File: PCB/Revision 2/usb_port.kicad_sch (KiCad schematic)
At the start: 1 part, among them J2 USB_A

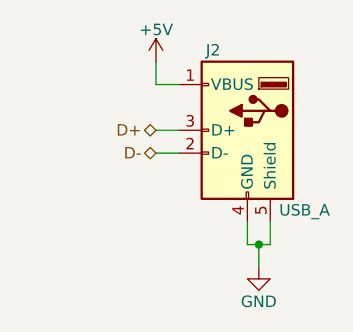
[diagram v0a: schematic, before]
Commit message: ESD protection diodes go BRRRRRRR
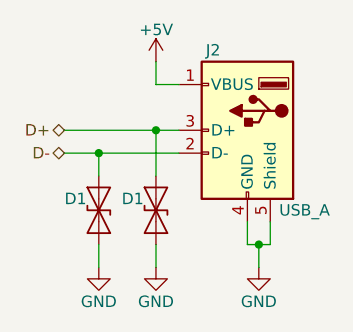
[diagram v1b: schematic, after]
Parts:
- added D1 (x2): ESD9B3.3ST5G, Diode_SMD:D_SOD-923, symbol Diode:ESD9B3.3ST5G
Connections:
- net D+: now also D1.1 (A1)
- net D-: now also D1.1 (A1)
- net GND: now also D1.2 (A2), D1.2 (A2)
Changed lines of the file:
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@@
 (kicad_sch (version 20230121) (generator eeschema)
   (paper "USLetter")
+  (junction (at 128.27 85.09) (diameter 0) (color 0 0 0 0)
+  )
+  (junction (at 121.92 87.63) (diameter 0) (color 0 0 0 0)
+  )
   (junction (at 139.7 97.79) (diameter 0) (color 0 0 0 0)
   )
@@
     (stroke (width 0) (type default))
   )
+  (wire (pts (xy 118.11 85.09) (xy 128.27 85.09))
+    (stroke (width 0) (type default))
+  )
+  (wire (pts (xy 128.27 85.09) (xy 128.27 90.17))
+    (stroke (width 0) (type default))
+  )
+  (wire (pts (xy 121.92 87.63) (xy 121.92 90.17))
+    (stroke (width 0) (type default))
+  )
+  (wire (pts (xy 121.92 97.79) (xy 121.92 100.33))
+    (stroke (width 0) (type default))
+  )
+  (wire (pts (xy 138.43 95.25) (xy 138.43 97.79))
+    (stroke (width 0) (type default))
+  )
+  (wire (pts (xy 118.11 87.63) (xy 121.92 87.63))
+    (stroke (width 0) (type default))
+  )
+  (wire (pts (xy 128.27 97.79) (xy 128.27 100.33))
+    (stroke (width 0) (type default))
+  )
   (wire (pts (xy 128.27 85.09) (xy 130.81 85.09))
     (stroke (width 0) (type default))
   )
-  (wire (pts (xy 138.43 95.25) (xy 138.43 97.79))
-    (stroke (width 0) (type default))
-  )
   (wire (pts (xy 138.43 97.79) (xy 139.7 97.79))
     (stroke (width 0) (type default))
   )
+  (wire (pts (xy 121.92 87.63) (xy 130.81 87.63))
+    (stroke (width 0) (type default))
+  )
   (wire (pts (xy 140.97 95.25) (xy 140.97 97.79))
     (stroke (width 0) (type default))
@@
     (stroke (width 0) (type default))
   )
-  (wire (pts (xy 128.27 87.63) (xy 130.81 87.63))
-    (stroke (width 0) (type default))
-  )
   (wire (pts (xy 128.27 80.01) (xy 130.81 80.01))
     (stroke (width 0) (type default))
@@
     (stroke (width 0) (type default))
   )
-  (hierarchical_label "D-" (shape bidirectional) (at 128.27 87.63 180) (fields_autoplaced)
+  (hierarchical_label "D-" (shape bidirectional) (at 118.11 87.63 180) (fields_autoplaced)
     (effects (font (size 1.27 1.27)) (justify right))
   )
-  (hierarchical_label "D+" (shape bidirectional) (at 128.27 85.09 180) (fields_autoplaced)
+  (hierarchical_label "D+" (shape bidirectional) (at 118.11 85.09 180) (fields_autoplaced)
     (effects (font (size 1.27 1.27)) (justify right))
+  )
+  (symbol (lib_id "power:GND") (at 128.27 100.33 0) (unit 1)
+    (in_bom yes) (on_board yes) (dnp no)
+    (property "Reference" "#PWR031" (at 128.27 106.68 0)
+      (effects (font (size 1.27 1.27)) hide)
+    )
+    (property "Value" "GND" (at 128.27 104.14 0)
+      (effects (font (size 1.27 1.27)))
+    )
+    (property "Footprint" "" (at 128.27 100.33 0)
+      (effects (font (size 1.27 1.27)) hide)
+    )
+    (property "Datasheet" "" (at 128.27 100.33 0)
+      (effects (font (size 1.27 1.27)) hide)
+    )
+    (pin "1")
+    (instances
+      (project "Revision 2"
+        (path "/3ba39048-ccb5-49b6-bc29-f9a8dd2e53b6"
+          (reference "#PWR031") (unit 1)
+        )
+        (path "/3ba39048-ccb5-49b6-bc29-f9a8dd2e53b6/ef7f0437-b22e-4c24-9273-d90d53267996"
+          (reference "#PWR0154") (unit 1)
+        )
+        (path "/3ba39048-ccb5-49b6-bc29-f9a8dd2e53b6/05c17752-4e2f-4780-999c-64683914a9ff"
+          (reference "#PWR0168") (unit 1)
+        )
+        (path "/3ba39048-ccb5-49b6-bc29-f9a8dd2e53b6/c07b2ed0-3ddf-4a7b-83a6-b9bc424f9605"
+          (reference "#PWR0177") (unit 1)
+        )
+        (path "/3ba39048-ccb5-49b6-bc29-f9a8dd2e53b6/82d9e5ae-142a-4573-82b3-b6ba579b1871"
+          (reference "#PWR0181") (unit 1)
+        )
+      )
+    )
+  )
+  (symbol (lib_id "Diode:ESD9B3.3ST5G") (at 128.27 93.98 270) (unit 1)
+    (in_bom yes) (on_board yes) (dnp no)
+    (property "Reference" "D1" (at 124.46 92.7099 90)
+      (effects (font (size 1.27 1.27)) (justify left))
+    )
+    (property "Value" "ESD9B3.3ST5G" (at 130.81 95.2499 90)
+      (effects (font (size 1.27 1.27)) (justify left) hide)
+    )
+    (property "Footprint" "Diode_SMD:D_SOD-923" (at 128.27 93.98 0)
+      (effects (font (size 1.27 1.27)) hide)
+    )
+    (property "Datasheet" "https://www.onsemi.com/pub/Collateral/ESD9B-D.PDF" (at 128.27 93.98 0)
+      (effects (font (size 1.27 1.27)) hide)
+    )
+    (pin "1")
+    (pin "2")
+    (instances
+      (project "Revision 2"
+        (path "/3ba39048-ccb5-49b6-bc29-f9a8dd2e53b6/e0049583-c97a-4b82-a4d7-59c894eac2f8"
+          (reference "D1") (unit 1)
+        )
+        (path "/3ba39048-ccb5-49b6-bc29-f9a8dd2e53b6/ef7f0437-b22e-4c24-9273-d90d53267996"
+          (reference "D1") (unit 1)
+        )
+        (path "/3ba39048-ccb5-49b6-bc29-f9a8dd2e53b6/05c17752-4e2f-4780-999c-64683914a9ff"
+          (reference "D18") (unit 1)
+        )
+        (path "/3ba39048-ccb5-49b6-bc29-f9a8dd2e53b6/c07b2ed0-3ddf-4a7b-83a6-b9bc424f9605"
+          (reference "D27") (unit 1)
+        )
+        (path "/3ba39048-ccb5-49b6-bc29-f9a8dd2e53b6/82d9e5ae-142a-4573-82b3-b6ba579b1871"
+          (reference "D31") (unit 1)
+        )
+      )
+    )
   )
   (symbol (lib_id "power:+5V") (at 128.27 77.47 0) (unit 1)
@@
     )
   )
+  (symbol (lib_id "Diode:ESD9B3.3ST5G") (at 121.92 93.98 270) (unit 1)
+    (in_bom yes) (on_board yes) (dnp no)
+    (property "Reference" "D1" (at 118.11 92.7099 90)
+      (effects (font (size 1.27 1.27)) (justify left))
+    )
+    (property "Value" "ESD9B3.3ST5G" (at 124.46 95.2499 90)
+      (effects (font (size 1.27 1.27)) (justify left) hide)
+    )
+    (property "Footprint" "Diode_SMD:D_SOD-923" (at 121.92 93.98 0)
+      (effects (font (size 1.27 1.27)) hide)
+    )
+    (property "Datasheet" "https://www.onsemi.com/pub/Collateral/ESD9B-D.PDF" (at 121.92 93.98 0)
+      (effects (font (size 1.27 1.27)) hide)
+    )
+    (pin "1")
+    (pin "2")
+    (instances
+      (project "Revision 2"
+        (path "/3ba39048-ccb5-49b6-bc29-f9a8dd2e53b6/e0049583-c97a-4b82-a4d7-59c894eac2f8"
+          (reference "D1") (unit 1)
+        )
+        (path "/3ba39048-ccb5-49b6-bc29-f9a8dd2e53b6/ef7f0437-b22e-4c24-9273-d90d53267996"
+          (reference "D1") (unit 1)
+        )
+        (path "/3ba39048-ccb5-49b6-bc29-f9a8dd2e53b6/05c17752-4e2f-4780-999c-64683914a9ff"
+          (reference "D18") (unit 1)
+        )
+        (path "/3ba39048-ccb5-49b6-bc29-f9a8dd2e53b6/c07b2ed0-3ddf-4a7b-83a6-b9bc424f9605"
+          (reference "D27") (unit 1)
+        )
+        (path "/3ba39048-ccb5-49b6-bc29-f9a8dd2e53b6/82d9e5ae-142a-4573-82b3-b6ba579b1871"
+          (reference "D30") (unit 1)
+        )
+      )
+    )
+  )
   (symbol (lib_id "power:GND") (at 139.7 100.33 0) (unit 1)
     (in_bom yes) (on_board yes) (dnp no)
@@
         )
       )
+    )
+  )
+  (symbol (lib_id "power:GND") (at 121.92 100.33 0) (unit 1)
+    (in_bom yes) (on_board yes) (dnp no)
+    (property "Reference" "#PWR031" (at 121.92 106.68 0)
+      (effects (font (size 1.27 1.27)) hide)
+    )
+    (property "Value" "GND" (at 121.92 104.14 0)
+      (effects (font (size 1.27 1.27)))
+    )
+    (property "Footprint" "" (at 121.92 100.33 0)
+      (effects (font (size 1.27 1.27)) hide)
+    )
+    (property "Datasheet" "" (at 121.92 100.33 0)
+      (effects (font (size 1.27 1.27)) hide)
+    )
+    (pin "1")
+    (instances
+      (project "Revision 2"
+        (path "/3ba39048-ccb5-49b6-bc29-f9a8dd2e53b6"
+          (reference "#PWR031") (unit 1)
+        )
+        (path "/3ba39048-ccb5-49b6-bc29-f9a8dd2e53b6/ef7f0437-b22e-4c24-9273-d90d53267996"
+          (reference "#PWR0154") (unit 1)
+        )
+        (path "/3ba39048-ccb5-49b6-bc29-f9a8dd2e53b6/05c17752-4e2f-4780-999c-64683914a9ff"
+          (reference "#PWR0168") (unit 1)
+        )
+        (path "/3ba39048-ccb5-49b6-bc29-f9a8dd2e53b6/c07b2ed0-3ddf-4a7b-83a6-b9bc424f9605"
+          (reference "#PWR0177") (unit 1)
+        )
+        (path "/3ba39048-ccb5-49b6-bc29-f9a8dd2e53b6/82d9e5ae-142a-4573-82b3-b6ba579b1871"
+          (reference "#PWR0180") (unit 1)
+        )
+      )
